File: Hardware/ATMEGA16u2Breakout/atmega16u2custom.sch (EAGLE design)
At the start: 58 parts, among them IC10 74LVC1G125DCK, J3 USB-MICRO B, U1 ATMEGA8U2AU

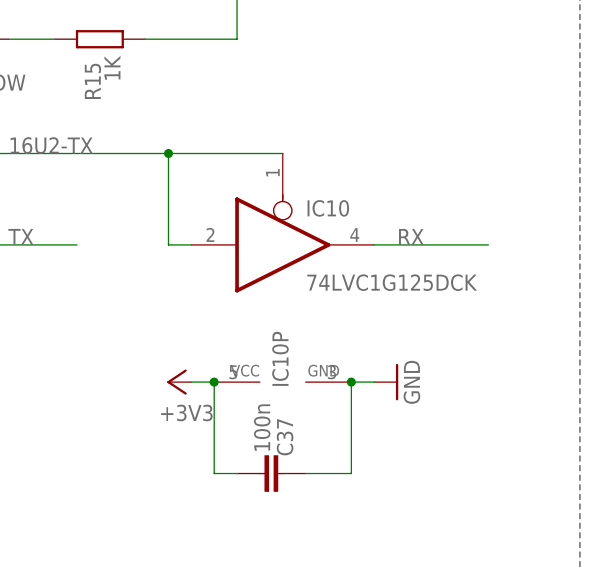
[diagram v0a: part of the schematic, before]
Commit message: atmega16u2 breakout board update
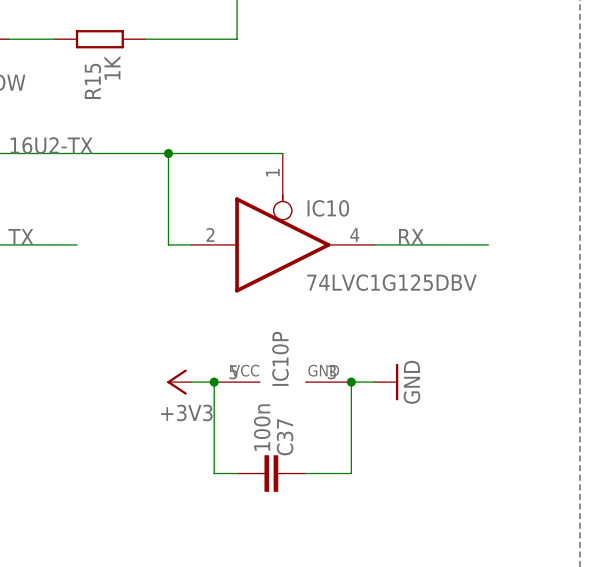
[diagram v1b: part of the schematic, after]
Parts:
- IC10: value 74LVC1G125DCK -> 74LVC1G125DBV; device 74xx-little-us:74LVC1G125DCK -> 74xx-little-us:74LVC1G125DBV
- Z3, Z4: device varistor:VARISTORCN0805 -> varistor:VARISTORCN0603
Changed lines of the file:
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@@
 <grid distance="0.1" unitdist="inch" unit="inch" style="lines" multiple="1" display="no" altdistance="0.01" altunitdist="inch" altunit="inch"/>
 <layers>
-<layer number="1" name="Top" color="4" fill="1" visible="no" active="no"/>
-<layer number="16" name="Bottom" color="1" fill="1" visible="no" active="no"/>
-<layer number="17" name="Pads" color="2" fill="1" visible="no" active="no"/>
-<layer number="18" name="Vias" color="14" fill="1" visible="no" active="no"/>
-<layer number="19" name="Unrouted" color="6" fill="1" visible="no" active="no"/>
-<layer number="20" name="Dimension" color="15" fill="1" visible="no" active="no"/>
-<layer number="21" name="tPlace" color="7" fill="1" visible="no" active="no"/>
-<layer number="22" name="bPlace" color="7" fill="1" visible="no" active="no"/>
-<layer number="23" name="tOrigins" color="15" fill="1" visible="no" active="no"/>
-<layer number="24" name="bOrigins" color="15" fill="1" visible="no" active="no"/>
-<layer number="25" name="tNames" color="7" fill="1" visible="no" active="no"/>
-<layer number="26" name="bNames" color="7" fill="1" visible="no" active="no"/>
-<layer number="27" name="tValues" color="7" fill="1" visible="no" active="no"/>
-<layer number="28" name="bValues" color="7" fill="1" visible="no" active="no"/>
-<layer number="29" name="tStop" color="2" fill="3" visible="no" active="no"/>
-<layer number="30" name="bStop" color="5" fill="6" visible="no" active="no"/>
+<layer number="1" name="Top" color="4" fill="1" visible="yes" active="no"/>
+<layer number="16" name="Bottom" color="1" fill="1" visible="yes" active="no"/>
+<layer number="17" name="Pads" color="2" fill="1" visible="yes" active="no"/>
+<layer number="18" name="Vias" color="2" fill="1" visible="yes" active="no"/>
+<layer number="19" name="Unrouted" color="6" fill="1" visible="yes" active="no"/>
+<layer number="20" name="Dimension" color="15" fill="1" visible="yes" active="no"/>
+<layer number="21" name="tPlace" color="7" fill="1" visible="yes" active="no"/>
+<layer number="22" name="bPlace" color="7" fill="1" visible="yes" active="no"/>
+<layer number="23" name="tOrigins" color="15" fill="1" visible="yes" active="no"/>
+<layer number="24" name="bOrigins" color="15" fill="1" visible="yes" active="no"/>
+<layer number="25" name="tNames" color="7" fill="1" visible="yes" active="no"/>
+<layer number="26" name="bNames" color="7" fill="1" visible="yes" active="no"/>
+<layer number="27" name="tValues" color="7" fill="1" visible="yes" active="no"/>
+<layer number="28" name="bValues" color="7" fill="1" visible="yes" active="no"/>
+<layer number="29" name="tStop" color="7" fill="3" visible="no" active="no"/>
+<layer number="30" name="bStop" color="7" fill="6" visible="no" active="no"/>
 <layer number="31" name="tCream" color="7" fill="4" visible="no" active="no"/>
 <layer number="32" name="bCream" color="7" fill="5" visible="no" active="no"/>
@@
 <layer number="35" name="tGlue" color="7" fill="4" visible="no" active="no"/>
 <layer number="36" name="bGlue" color="7" fill="5" visible="no" active="no"/>
-<layer number="37" name="tTest" color="7" fill="1" visible="no" active="no"/>
-<layer number="38" name="bTest" color="7" fill="1" visible="no" active="no"/>
+<layer number="37" name="tTest" color="7" fill="1" visible="yes" active="no"/>
+<layer number="38" name="bTest" color="7" fill="1" visible="yes" active="no"/>
 <layer number="39" name="tKeepout" color="4" fill="11" visible="no" active="no"/>
 <layer number="40" name="bKeepout" color="1" fill="11" visible="no" active="no"/>
@@
 <layer number="44" name="Drills" color="7" fill="1" visible="no" active="no"/>
 <layer number="45" name="Holes" color="7" fill="1" visible="no" active="no"/>
-<layer number="46" name="Milling" color="3" fill="1" visible="no" active="no"/>
-<layer number="47" name="Measures" color="7" fill="1" visible="no" active="no"/>
-<layer number="48" name="Document" color="7" fill="1" visible="no" active="no"/>
-<layer number="49" name="Reference" color="13" fill="1" visible="no" active="no"/>
-<layer number="50" name="dxf" color="12" fill="1" visible="no" active="no"/>
-<layer number="51" name="tDocu" color="7" fill="1" visible="no" active="no"/>
-<layer number="52" name="bDocu" color="7" fill="1" visible="no" active="no"/>
-<layer number="53" name="tGND_GNDA" color="7" fill="1" visible="no" active="no"/>
-<layer number="54" name="bGND_GNDA" color="7" fill="1" visible="no" active="no"/>
-<layer number="56" name="wert" color="7" fill="1" visible="no" active="no"/>
-<layer number="57" name="tCAD" color="7" fill="1" visible="no" active="no"/>
+<layer number="46" name="Milling" color="3" fill="1" visible="yes" active="no"/>
+<layer number="47" name="Measures" color="7" fill="1" visible="yes" active="no"/>
+<layer number="48" name="Document" color="7" fill="1" visible="yes" active="no"/>
+<layer number="49" name="Reference" color="7" fill="1" visible="yes" active="no"/>
+<layer number="50" name="dxf" color="12" fill="1" visible="yes" active="no"/>
+<layer number="51" name="tDocu" color="7" fill="1" visible="yes" active="no"/>
+<layer number="52" name="bDocu" color="7" fill="1" visible="yes" active="no"/>
+<layer number="53" name="tGND_GNDA" color="7" fill="1" visible="yes" active="no"/>
+<layer number="54" name="bGND_GNDA" color="7" fill="1" visible="yes" active="no"/>
+<layer number="56" name="wert" color="7" fill="1" visible="yes" active="no"/>
+<layer number="57" name="tCAD" color="7" fill="1" visible="yes" active="no"/>
 <layer number="90" name="Modules" color="5" fill="1" visible="yes" active="yes"/>
 <layer number="91" name="Nets" color="2" fill="1" visible="yes" active="yes"/>
@@
 <part name="GND39" library="supply1" deviceset="GND" device=""/>
 <part name="GND40" library="supply1" deviceset="GND" device=""/>
-<part name="Z3" library="varistor" deviceset="VARISTOR" device="CN0805" value="CG0603MLC-05E"/>
-<part name="Z4" library="varistor" deviceset="VARISTOR" device="CN0805" value="CG0603MLC-05E"/>
+<part name="Z3" library="varistor" deviceset="VARISTOR" device="CN0603" value="CG0603MLC-05E"/>
+<part name="Z4" library="varistor" deviceset="VARISTOR" device="CN0603" value="CG0603MLC-05E"/>
 <part name="R9" library="SmartPrj" deviceset="R-EU_" device="R0805" value="1M_NM"/>
 <part name="C39" library="SmartPrj" deviceset="C-EU" device="C0805" value="22p"/>
@@
 <part name="P+3" library="supply1" deviceset="+5V" device=""/>
 <part name="P+5" library="supply1" deviceset="+5V" device=""/>
-<part name="IC10" library="74xx-little-us" deviceset="74*1G125" device="DCK" technology="LVC"/>
+<part name="IC10" library="74xx-little-us" deviceset="74*1G125" device="DBV" technology="LVC" value="74LVC1G125DBV"/>
 <part name="R23" library="SmartPrj" deviceset="R-EU_" device="R0805" value="1K"/>
 <part name="GND30" library="supply1" deviceset="GND" device=""/>
